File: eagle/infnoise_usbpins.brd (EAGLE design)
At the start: 34.8 x 12.2 mm, 28 parts, among them SW1 MC74VHC1G66DFT1G, SW2 MC74VHC1G66DFT1G, X1 USBRAWPINS

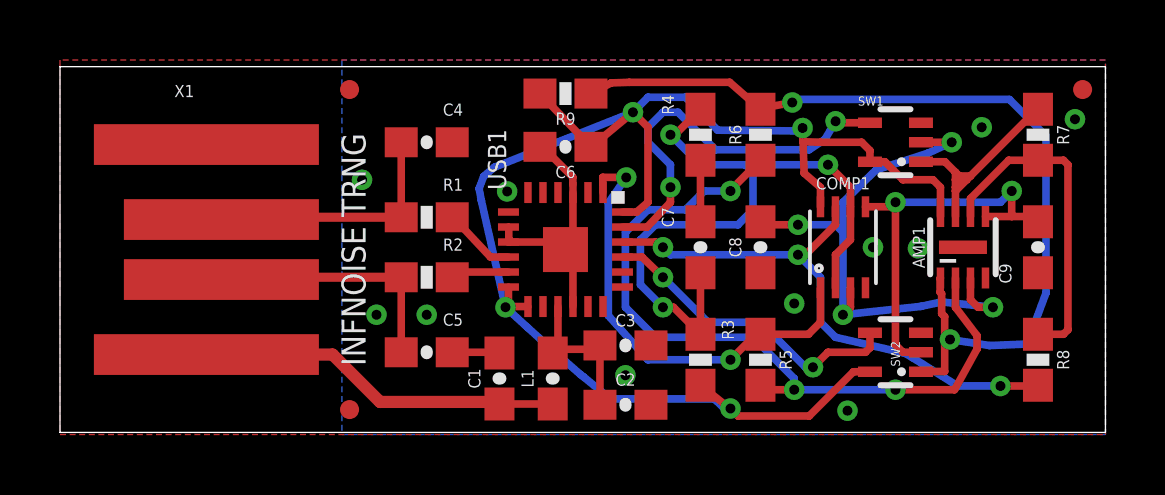
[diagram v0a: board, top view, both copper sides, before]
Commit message: Changed gain target to 1.84
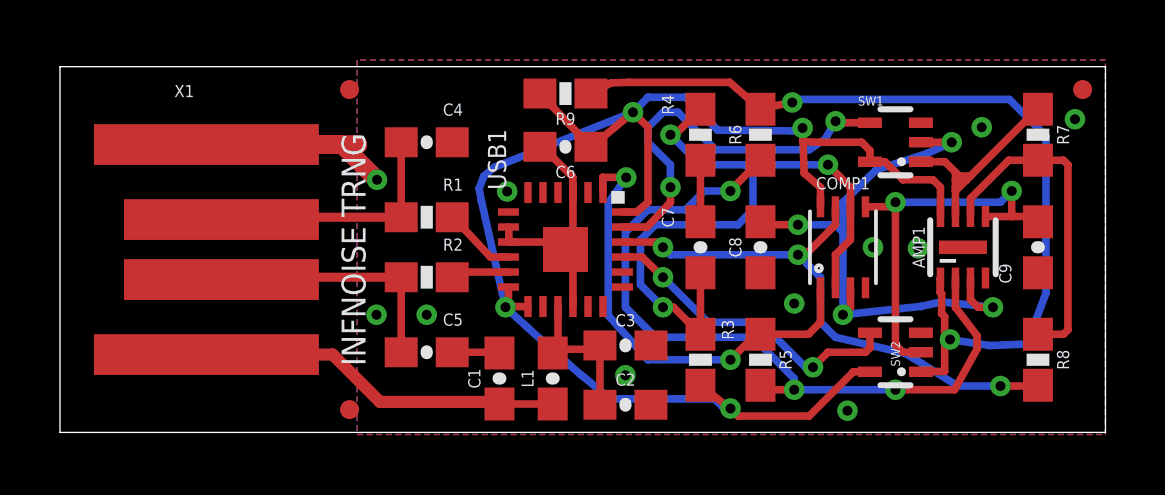
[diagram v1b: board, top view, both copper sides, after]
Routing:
- net GND: track 11.4 -> 19.2 mm
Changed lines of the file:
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@@
 <setting verticaltext="up"/>
 </settings>
-<grid distance="0.1" unitdist="mm" unit="mm" style="lines" multiple="1" display="yes" altdistance="0.125" altunitdist="mm" altunit="mm"/>
+<grid distance="1" unitdist="mil" unit="mil" style="lines" multiple="1" display="yes" altdistance="0.125" altunitdist="mm" altunit="mm"/>
 <layers>
 <layer number="1" name="Top" color="4" fill="1" visible="yes" active="yes"/>
@@
 <board>
 <plain>
-<text x="21.0566" y="6.3754" size="2.1844" layer="26" rot="MR0" align="center">Infinite Noise</text>
+<text x="23.3566" y="6.0754" size="2.1844" layer="26" rot="MR0" align="center">Infinite Noise</text>
 <text x="9.386" y="6.096" size="0.8" layer="25" rot="R90" align="top-center">INFNOISE TRNG</text>
 <wire x1="0" y1="0" x2="0" y2="12.192" width="0" layer="20"/>
@@
 <wire x1="5.4562" y1="7.1722" x2="11.3738" y2="7.1722" width="0.3048" layer="1"/>
 <contactref element="X1" pad="USB_P"/>
-<wire x1="5.38" y1="7.096" x2="5.4562" y2="7.1722" width="0" layer="19" extent="1-1"/>
+<wire x1="5.38" y1="7.096" x2="5.4562" y2="7.096" width="0.254" layer="1"/>
+<wire x1="5.4562" y1="7.096" x2="5.4562" y2="7.1722" width="0.254" layer="1"/>
 </signal>
 <signal name="USB_M">
@@
 <wire x1="5.4562" y1="5.1722" x2="11.3738" y2="5.1722" width="0.3048" layer="1"/>
 <contactref element="X1" pad="USB_M"/>
-<wire x1="5.38" y1="5.096" x2="5.4562" y2="5.1722" width="0" layer="19" extent="1-1"/>
+<wire x1="5.38" y1="5.096" x2="5.4562" y2="5.096" width="0.254" layer="1"/>
+<wire x1="5.4562" y1="5.096" x2="5.4562" y2="5.1722" width="0.254" layer="1"/>
 </signal>
 <signal name="VCCIN">
@@
 <contactref element="C7" pad="2"/>
 <polygon width="0.254" layer="16">
-<vertex x="9.398" y="12.4142"/>
-<vertex x="9.398" y="-0.0698"/>
+<vertex x="9.898" y="12.4142"/>
+<vertex x="9.898" y="-0.0698"/>
 <vertex x="34.8488" y="-0.0698"/>
 <vertex x="34.8488" y="12.4142"/>
 </polygon>
 <polygon width="0.254" layer="1">
-<vertex x="0" y="12.4142"/>
-<vertex x="0" y="-0.0698"/>
+<vertex x="9.906" y="12.4142"/>
+<vertex x="9.906" y="-0.0698"/>
 <vertex x="34.8488" y="-0.0698"/>
 <vertex x="34.8488" y="12.4142"/>
@@
 <wire x1="17.0988" y1="5.9222" x2="16.8488" y2="6.096" width="0.254" layer="1"/>
 <via x="10.5506" y="3.9222" extent="1-16" drill="0.3302"/>
-<via x="10.068" y="8.4222" extent="1-16" drill="0.3302"/>
+<via x="10.568" y="8.4222" extent="1-16" drill="0.3302"/>
 <wire x1="17.0988" y1="7.996" x2="17.0988" y2="6.4222" width="0.254" layer="1"/>
 <wire x1="17.0988" y1="6.4222" x2="16.8488" y2="6.096" width="0.254" layer="1"/>
@@
 <wire x1="17.0942" y1="8.509" x2="16.4084" y2="9.1948" width="0.254" layer="1"/>
 <contactref element="X1" pad="GND"/>
-<wire x1="17.0988" y1="7.996" x2="17.0942" y2="8.255" width="0" layer="19" extent="1-1"/>
+<wire x1="17.0942" y1="8.255" x2="17.0988" y2="8.255" width="0.254" layer="1"/>
+<wire x1="17.0988" y1="8.255" x2="17.0988" y2="7.996" width="0.254" layer="1"/>
+<wire x1="4.88" y1="9.596" x2="9.3942" y2="9.596" width="0.6096" layer="1"/>
+<wire x1="9.3942" y1="9.596" x2="10.568" y2="8.4222" width="0.6096" layer="1"/>
+<wire x1="8.5598" y1="9.6012" x2="9.9314" y2="9.6012" width="0.6096" layer="1"/>
+<wire x1="9.9314" y1="9.6012" x2="9.9314" y2="9.5758" width="0.6096" layer="1"/>
 </signal>
 <signal name="VCC33">
